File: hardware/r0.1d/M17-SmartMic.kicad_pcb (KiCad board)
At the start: 4 copper layers, 84.9 x 89.9 mm, 180 parts, among them IC1 LM4861M, J1 Kenwood-2.5, J10 UART, J11 Radio_Opt, J2 USB_C, J3 OLED, J4 CAT_TX, J5 Kenwood-3.5, J6 CAT_TX, J7 Radio, J8 +12V, J9 STLink, Q1 IRLML2060, Q2 BSS138, Q3 BSS138, SW1 Button Up, SW2 Button Down, SW3 Reset, SW4 Button Escape, SW5 Button Left, SW6 Button Enter, SW7 Button Right, U1 MAX9814, U10 STM32F405RGTx, U11 TPS73233, U2 TP6841S6, U3 USBLC6-2, U6 MCP6002, U7 MCP6002, U8 MCP4551-103, U9 MCP4551-104, X1 12 MHz TCXO, Y1 8 MHz

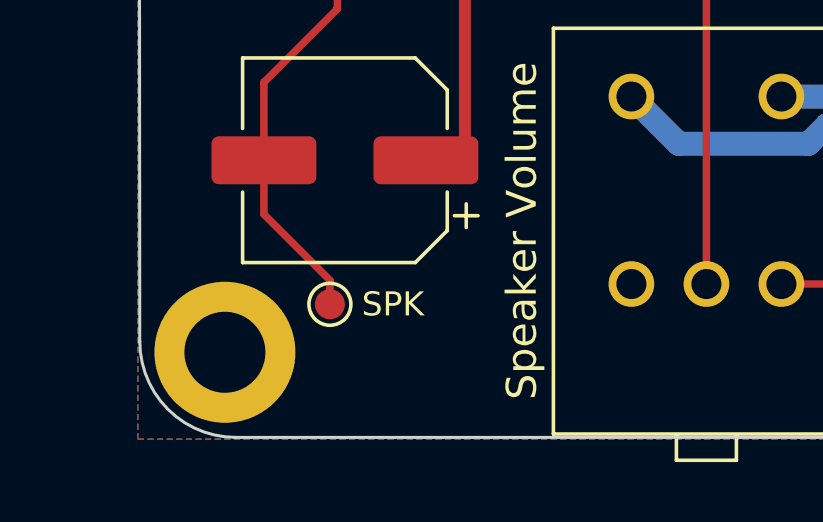
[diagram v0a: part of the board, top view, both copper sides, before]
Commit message: Update r0.1d
Added speaker connector, beautified silk screen
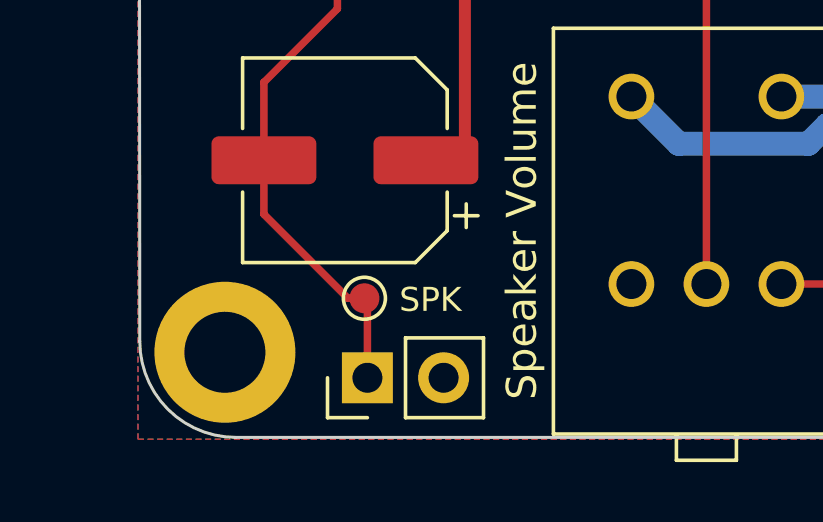
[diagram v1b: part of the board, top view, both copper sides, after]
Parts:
- added J12: Speaker, Connector_PinHeader_2.54mm:PinHeader_1x02_P2.54mm_Vertical, F.Cu at (76.8, 122.0)
- moved TP4 1.17 mm to (76.7, 119.3)
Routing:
- net SPEAKER: track 13.0 -> 16.3 mm
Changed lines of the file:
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@@
+    )
+  )
+  (footprint "Connector_PinHeader_2.54mm:PinHeader_1x02_P2.54mm_Vertical" (layer "F.Cu")
+    (at 76.75 121.95 90)
+    (descr "Through hole straight pin header, 1x02, 2.54mm pitch, single row")
+    (tags "Through hole pin header THT 1x02 2.54mm single row")
+    (property "Sheetfile" "Audio.kicad_sch")
+    (property "Sheetname" "Audio & Filter")
+    (attr through_hole)
+    (fp_text reference "J12" (at 0 -2.33 90) (layer "F.Fab")
+      (effects (font (size 1 1) (thickness 0.15)))
+    )
+    (fp_text value "Speaker" (at 0 4.87 90) (layer "F.Fab")
+      (effects (font (size 1 1) (thickness 0.15)))
+    )
+    (fp_text user "${REFERENCE}" (at 0 1.27) (layer "F.Fab")
+      (effects (font (size 1 1) (thickness 0.15)))
+    )
+    (fp_line (start -1.33 3.87) (end 1.33 3.87) (layer "F.SilkS") (width 0.12))
+    (fp_line (start 1.33 1.27) (end 1.33 3.87) (layer "F.SilkS") (width 0.12))
+    (fp_line (start -1.33 -1.33) (end 0 -1.33) (layer "F.SilkS") (width 0.12))
+    (fp_line (start -1.33 1.27) (end 1.33 1.27) (layer "F.SilkS") (width 0.12))
+    (fp_line (start -1.33 1.27) (end -1.33 3.87) (layer "F.SilkS") (width 0.12))
+    (fp_line (start -1.33 0) (end -1.33 -1.33) (layer "F.SilkS") (width 0.12))
+    (fp_line (start 1.8 -1.8) (end -1.8 -1.8) (layer "F.CrtYd") (width 0.05))
+    (fp_line (start -1.8 -1.8) (end -1.8 4.35) (layer "F.CrtYd") (width 0.05))
+    (fp_line (start -1.8 4.35) (end 1.8 4.35) (layer "F.CrtYd") (width 0.05))
+    (fp_line (start 1.8 4.35) (end 1.8 -1.8) (layer "F.CrtYd") (width 0.05))
+    (fp_line (start 1.27 3.81) (end -1.27 3.81) (layer "F.Fab") (width 0.1))
+    (fp_line (start -1.27 3.81) (end -1.27 -0.635) (layer "F.Fab") (width 0.1))
+    (fp_line (start -1.27 -0.635) (end -0.635 -1.27) (layer "F.Fab") (width 0.1))
+    (fp_line (start -0.635 -1.27) (end 1.27 -1.27) (layer "F.Fab") (width 0.1))
+    (fp_line (start 1.27 -1.27) (end 1.27 3.81) (layer "F.Fab") (width 0.1))
+    (pad "1" thru_hole rect (at 0 0 90) (size 1.7 1.7) (drill 1) (layers *.Cu *.Mask)
+      (net 39 "SPEAKER") (pinfunction "Pin_1") (pintype "passive"))
+    (pad "2" thru_hole oval (at 0 2.54 90) (size 1.7 1.7) (drill 1) (layers *.Cu *.Mask)
+      (net 2 "GND") (pinfunction "Pin_2") (pintype "passive"))
+    (model "${KICAD6_3DMODEL_DIR}/Connector_PinHeader_2.54mm.3dshapes/PinHeader_1x02_P2.54mm_Vertical.wrl"
+      (offset (xyz 0 0 0))
+      (scale (xyz 1 1 1))
+      (rotate (xyz 0 0 0))
     )
   )
@@
   )
   (footprint "TestPoint:TestPoint_Pad_D1.0mm" (layer "F.Cu")
-    (at 75.5 119.5)
+    (at 76.65 119.3)
     (descr "SMD pad as test Point, diameter 1.0mm")
     (tags "test point SMD pad")
@@
     (effects (font (size 1 1) (thickness 0.15)) (justify mirror))
   )
-  (gr_text "CTX" (at 95.3 49.5) (layer "B.SilkS")
+  (gr_text "CAT TX" (at 94.2 50.3 45) (layer "B.SilkS")
     (effects (font (size 0.8 0.8) (thickness 0.12)) (justify mirror))
   )
@@
     (effects (font (size 1 1) (thickness 0.15)) (justify mirror))
   )
-  (gr_text "RX" (at 84.9 49.5) (layer "B.SilkS")
+  (gr_text "RX" (at 84.9 49.5 45) (layer "B.SilkS")
     (effects (font (size 0.8 0.8) (thickness 0.12)) (justify mirror))
   )
-  (gr_text "PTT" (at 90.2 49.5) (layer "B.SilkS")
+  (gr_text "PTT" (at 90.2 49.5 45) (layer "B.SilkS")
     (effects (font (size 0.8 0.8) (thickness 0.12)) (justify mirror))
   )
@@
     (effects (font (size 1 1) (thickness 0.15)) (justify mirror))
   )
-  (gr_text "TX" (at 87.6 49.5) (layer "B.SilkS")
+  (gr_text "TX" (at 87.6 49.5 45) (layer "B.SilkS")
     (effects (font (size 0.8 0.8) (thickness 0.12)) (justify mirror))
   )
@@
     (effects (font (size 1 1) (thickness 0.15)) (justify mirror))
   )
-  (gr_text "GND" (at 97.7 49.5) (layer "B.SilkS")
+  (gr_text "GND" (at 97.7 49.5 45) (layer "B.SilkS")
     (effects (font (size 0.8 0.8) (thickness 0.12)) (justify mirror))
   )
@@
     (effects (font (size 1 1) (thickness 0.15)) (justify mirror))
   )
-  (gr_text "CRX" (at 92.7 49.5) (layer "B.SilkS")
+  (gr_text "CAT RX" (at 91.6 50.35 45) (layer "B.SilkS")
     (effects (font (size 0.8 0.8) (thickness 0.12)) (justify mirror))
   )
@@
     (effects (font (size 1 1) (thickness 0.15)) (justify left))
   )
-  (gr_text "SPK" (at 77.6 119.5) (layer "F.SilkS")
+  (gr_text "SPK" (at 78.85 119.35) (layer "F.SilkS")
     (effects (font (size 0.8 0.8) (thickness 0.12)))
   )
@@
   (segment (start 83.5 92.85) (end 81.75 92.85) (width 0.25) (layer "F.Cu") (net 38))
   (segment (start 83.5 97.05) (end 82.35 97.05) (width 0.25) (layer "F.Cu") (net 38))
-  (segment (start 75.5 118.7) (end 73.3 116.5) (width 0.25) (layer "F.Cu") (net 39))
+  (segment (start 76.75 119.4) (end 76.65 119.3) (width 0.25) (layer "F.Cu") (net 39))
+  (segment (start 76.75 121.95) (end 76.75 119.4) (width 0.25) (layer "F.Cu") (net 39))
+  (segment (start 76.65 119.3) (end 76.1 119.3) (width 0.25) (layer "F.Cu") (net 39))
   (segment (start 75.75 109.65) (end 75.75 108.4) (width 0.25) (layer "F.Cu") (net 39))
   (segment (start 73.3 116.5) (end 73.3 114.7) (width 0.25) (layer "F.Cu") (net 39))
   (segment (start 73.3 112.1) (end 75.75 109.65) (width 0.25) (layer "F.Cu") (net 39))
-  (segment (start 75.5 119.5) (end 75.5 118.7) (width 0.25) (layer "F.Cu") (net 39))
   (segment (start 73.3 114.7) (end 73.3 112.1) (width 0.25) (layer "F.Cu") (net 39))
+  (segment (start 76.1 119.3) (end 73.3 116.5) (width 0.25) (layer "F.Cu") (net 39))
   (segment (start 92.055 54.775) (end 93.355 54.775) (width 0.25) (layer "F.Cu") (net 40))
   (segment (start 93.805 56.325) (end 93.805 55.325) (width 0.25) (layer "F.Cu") (net 40))
